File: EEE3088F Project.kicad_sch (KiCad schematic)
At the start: 83 parts, among them J1 Conn_02x16_Odd_Even, J2 Battery IN JST, M1BulkC1 10uF, M1Control1 DRV8837, M2BulkC1 10uF, M2Control1 DRV8837, M3BC1 BCM3_JP, M3BulkC1 10uF, M3Control1 DRV8837, M4BulkC1 10uF, M4Control1 DRV8837, Q2 AO3400A

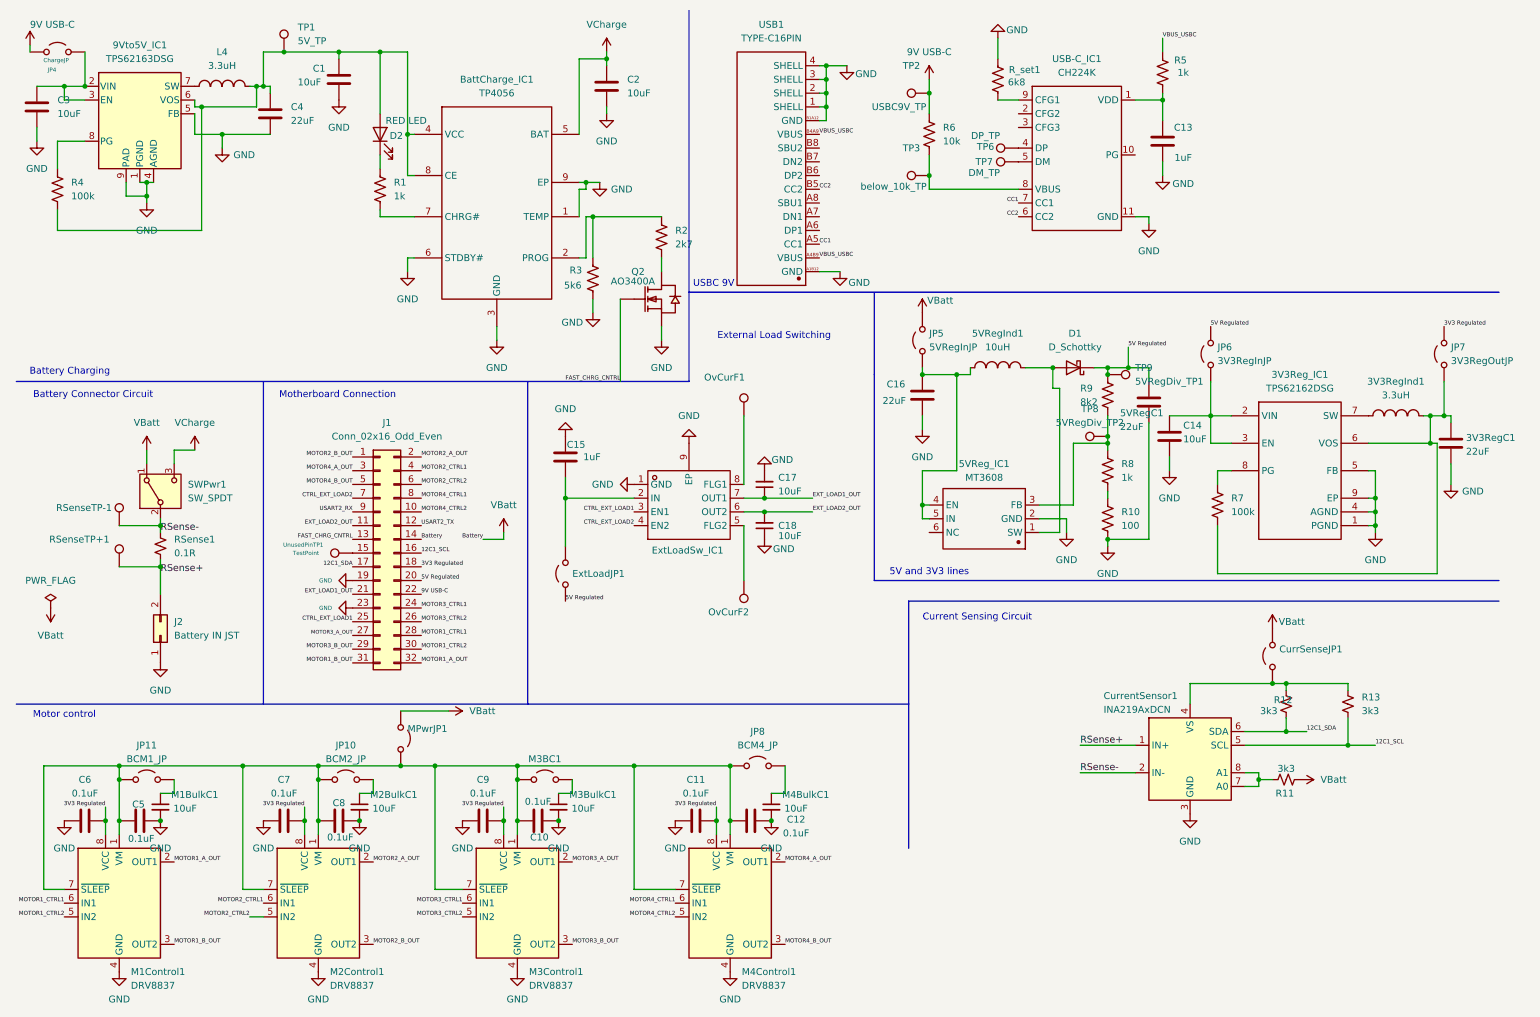
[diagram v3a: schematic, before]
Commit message: Minor labelling fixes. Generated gerber files
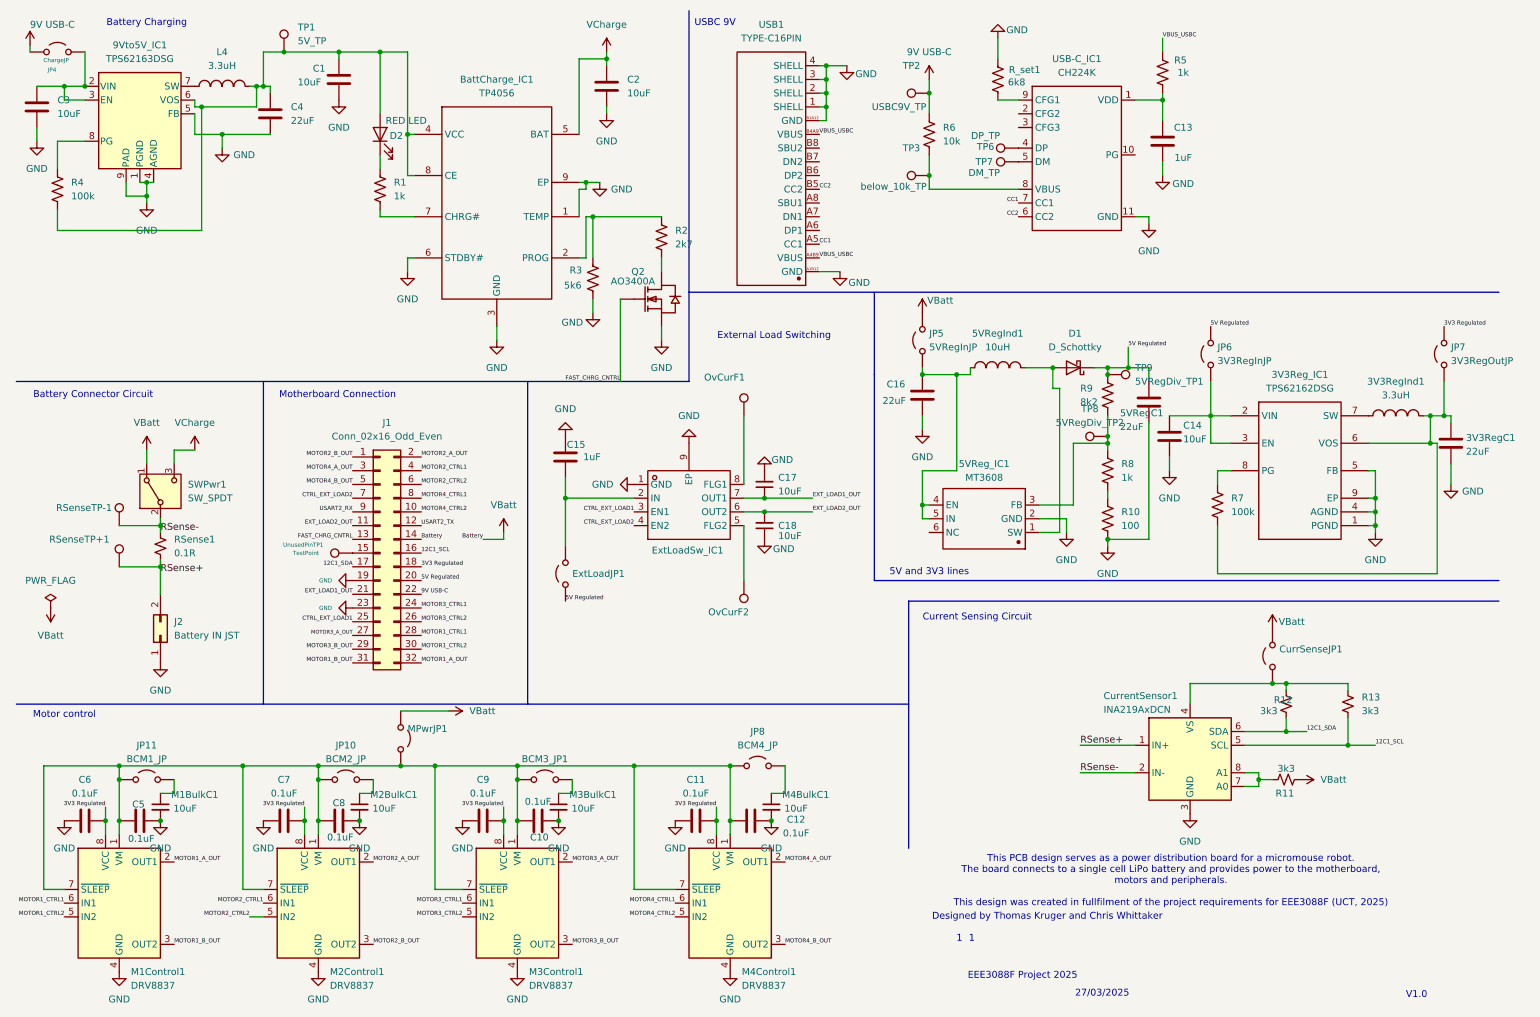
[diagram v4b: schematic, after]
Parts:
- renumbered M3BC1 to BCM3_JP1
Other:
- note added: "1"
- note added: "27/03/2025"
- note added: "Designed by Thomas Kruger and Chris Whittaker"
- note added: "EEE3088F Project 2025"
- note added: "This PCB design serves as a power distribution board for a micromouse robot. The board connects to a single cell LiPo battery and provides power to the motherboard, motors and peripherals. This design was created in fullfilment of the project requirements for EEE3088F (UCT, 2025)"
- note added: "V1.0"
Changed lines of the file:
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@@
 	(generator_version "9.0")
 	(paper "A4")
+	(text "1\n"
+		(exclude_from_sim no)
+		(at 185.928 183.134 0)
+		(effects
+			(font
+				(size 1.27 1.27)
+			)
+		)
+	)
 	(text "Motor control\n"
 		(exclude_from_sim no)
@@
 		)
 	)
+	(text "27/03/2025\n"
+		(exclude_from_sim no)
+		(at 212.344 193.294 0)
+		(effects
+			(font
+				(size 1.27 1.27)
+			)
+		)
+	)
 	(text "External Load Switching\n"
 		(exclude_from_sim no)
@@
 		)
 	)
+	(text "V1.0\n"
+		(exclude_from_sim no)
+		(at 270.51 193.548 0)
+		(effects
+			(font
+				(size 1.27 1.27)
+			)
+		)
+	)
 	(text "USBC 9V"
 		(exclude_from_sim no)
-		(at 140.462 61.976 0)
+		(at 140.716 13.716 0)
 		(effects
 			(font
@@
 	(text "Battery Charging"
 		(exclude_from_sim no)
-		(at 21.336 78.232 0)
+		(at 35.56 13.716 0)
 		(effects
 			(font
@@
 		)
 	)
+	(text "EEE3088F Project 2025\n"
+		(exclude_from_sim no)
+		(at 197.612 189.992 0)
+		(effects
+			(font
+				(size 1.27 1.27)
+			)
+		)
+	)
+	(text "1\n"
+		(exclude_from_sim no)
+		(at 188.214 183.134 0)
+		(effects
+			(font
+				(size 1.27 1.27)
+			)
+		)
+	)
 	(text "Motherboard Connection\n"
 		(exclude_from_sim no)
@@
 		)
 	)
+	(text "Designed by Thomas Kruger and Chris Whittaker\n"
+		(exclude_from_sim no)
+		(at 202.184 179.07 0)
+		(effects
+			(font
+				(size 1.27 1.27)
+			)
+		)
+	)
 	(text "Current Sensing Circuit\n"
 		(exclude_from_sim no)
@@
 		)
 	)
+	(text "This PCB design serves as a power distribution board for a micromouse robot.\nThe board connects to a single cell LiPo battery and provides power to the motherboard,\nmotors and peripherals.\n\nThis design was created in fullfilment of the project requirements for EEE3088F (UCT, 2025)"
+		(exclude_from_sim no)
+		(at 225.044 172.466 0)
+		(effects
+			(font
+				(size 1.27 1.27)
+			)
+			(href "#1")
+		)
+	)
 	(junction
 		(at 262.89 104.14)
@@
 		(dnp no)
 		(fields_autoplaced yes)
-		(property "Reference" "M3BC1"
+		(property "Reference" "BCM3_JP1"
 			(at 109.22 149.86 0)
 			(effects
@@
 			(project ""
 				(path "/bbd0b894-fd60-489b-a5d2-e477407ae42a"
-					(reference "M3BC1")
+					(reference "BCM3_JP1")
 					(unit 1)
 				)
